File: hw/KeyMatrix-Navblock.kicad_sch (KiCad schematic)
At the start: 52 parts, among them SW4300 SW_Cherry_MX_RGB, SW4301 SW_Cherry_MX_RGB, SW4302 SW_Cherry_MX_RGB, SW4303 SW_Cherry_MX_RGB, SW4304 SW_Cherry_MX_RGB, SW4305 SW_Cherry_MX_RGB, SW4306 SW_Cherry_MX_RGB, SW4307 SW_Cherry_MX_RGB, SW4308 SW_Cherry_MX_RGB, SW4309 SW_Cherry_MX_RGB, SW4310 SW_Cherry_MX_RGB, SW4311 SW_Cherry_MX_RGB, SW4312 SW_Cherry_MX_RGB, SW4313 SW_Cherry_MX_RGB, SW4314 SW_Cherry_MX_RGB, X4300 Keycap-R1-1x1, X4301 Keycap-R1-1x1, X4302 Keycap-R1-1x1, X4303 Keycap-R1-1x1, X4304 Keycap-R1-1x1, X4305 Keycap-R1-1x1, X4306 Keycap-R1-1x1, X4307 Keycap-R1-1x1, X4308 Keycap-R1-1x1, X4309 Keycap-R1-1x1, X4310 Keycap-R1-1x1, X4311 Keycap-R1-1x1, X4312 Keycap-R1-1x1, X4313 Keycap-R1-1x1, X4314 Keycap-R1-1x1

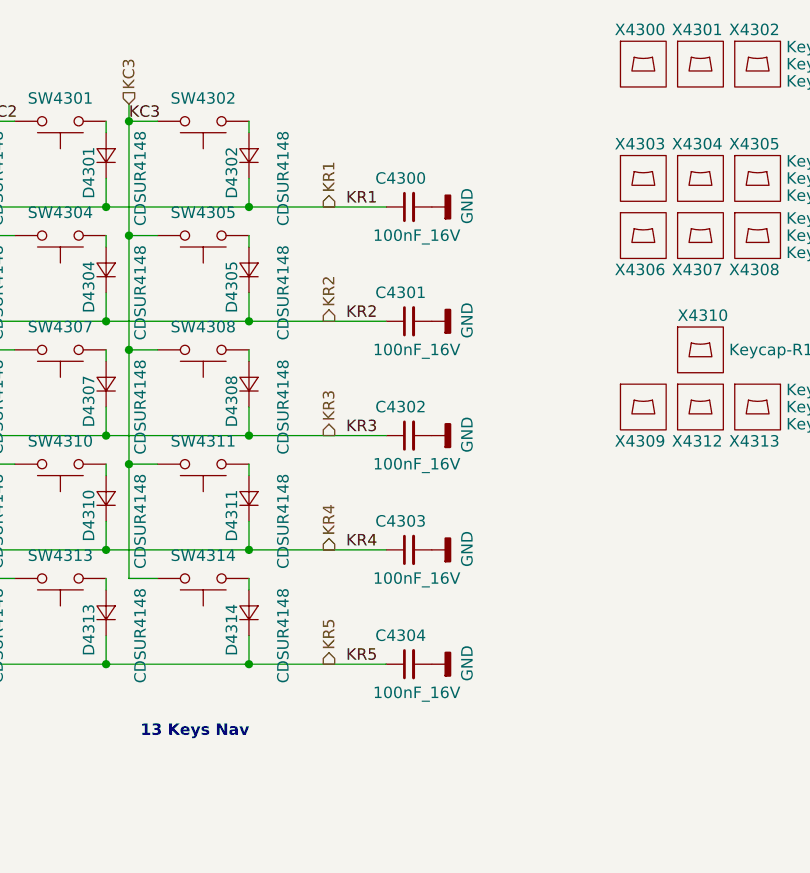
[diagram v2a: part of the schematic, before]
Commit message: Change key matrix capacitors to 220pF.
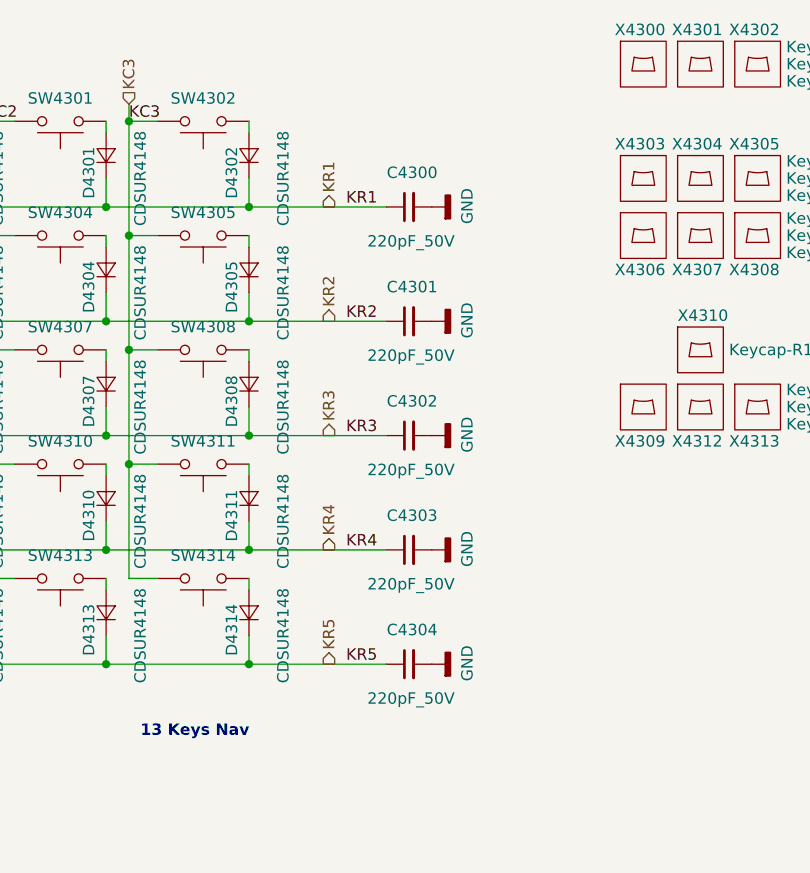
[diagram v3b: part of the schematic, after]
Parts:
- removed C4300, C4301, C4302, C4303, C4304: 100nF_16V, Keyboard:C_0402, symbol Keyboard:100nF_16V
- added C4300, C4301, C4302, C4303, C4304: 220pF_50V, Keyboard:C_0402, symbol Keyboard:220pF_50V
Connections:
- net GND: now also C4300.2, C4301.2, C4302.2, C4303.2, C4304.2
- net KR1: now also C4300.1
- net KR2: now also C4301.1
- net KR3: now also C4302.1
- net KR4: now also C4303.1
- net KR5: now also C4304.1
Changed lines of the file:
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@@
-    (pin "2")
-  )
-  (symbol (lib_id "Keyboard:100nF_16V") (at 88.265 98.425 90) (unit 1)
-    (in_bom yes) (on_board yes)
-    (property "Reference" "C4304" (id 0) (at 90.17 95.25 90)
-      (effects (font (size 1.27 1.27)) (justify left))
-    )
-    (property "Value" "100nF_16V" (id 1) (at 93.98 101.6 90)
-      (effects (font (size 1.27 1.27)) (justify left))
-    )
-    (property "Footprint" "Keyboard:C_0402" (id 2) (at 89.027 100.711 0)
-      (effects (font (size 1.27 1.27)) hide)
-    )
-    (property "Datasheet" "80-C0402C104K4R" (id 3) (at 86.487 98.171 0)
-      (effects (font (size 1.27 1.27)) hide)
-    )
-    (property "mouser#" "80-C0402C104K4R" (id 4) (at 83.947 95.631 0)
-      (effects (font (size 1.524 1.524)) hide)
-    )
-    (pin "1")
     (pin "2")
   )
@@
     (pin "2")
   )
-  (symbol (lib_id "Keyboard:100nF_16V") (at 88.265 60.325 90) (unit 1)
-    (in_bom yes) (on_board yes)
-    (property "Reference" "C4301" (id 0) (at 90.17 57.15 90)
-      (effects (font (size 1.27 1.27)) (justify left))
-    )
-    (property "Value" "100nF_16V" (id 1) (at 93.98 63.5 90)
-      (effects (font (size 1.27 1.27)) (justify left))
-    )
-    (property "Footprint" "Keyboard:C_0402" (id 2) (at 89.027 62.611 0)
-      (effects (font (size 1.27 1.27)) hide)
-    )
-    (property "Datasheet" "80-C0402C104K4R" (id 3) (at 86.487 60.071 0)
-      (effects (font (size 1.27 1.27)) hide)
-    )
-    (property "mouser#" "80-C0402C104K4R" (id 4) (at 83.947 57.531 0)
-      (effects (font (size 1.524 1.524)) hide)
-    )
-    (pin "1")
-    (pin "2")
-  )
   (symbol (lib_id "Keyboard:SW_Cherry_MX_RGB") (at 33.655 38.1 0) (mirror x) (unit 1)
     (in_bom yes) (on_board yes)
@@
     (pin "2")
   )
-  (symbol (lib_id "Keyboard:100nF_16V") (at 88.265 47.625 90) (unit 1)
-    (in_bom yes) (on_board yes)
-    (property "Reference" "C4300" (id 0) (at 90.17 44.45 90)
-      (effects (font (size 1.27 1.27)) (justify left))
-    )
-    (property "Value" "100nF_16V" (id 1) (at 93.98 50.8 90)
-      (effects (font (size 1.27 1.27)) (justify left))
-    )
-    (property "Footprint" "Keyboard:C_0402" (id 2) (at 89.027 49.911 0)
-      (effects (font (size 1.27 1.27)) hide)
-    )
-    (property "Datasheet" "80-C0402C104K4R" (id 3) (at 86.487 47.371 0)
-      (effects (font (size 1.27 1.27)) hide)
-    )
-    (property "mouser#" "80-C0402C104K4R" (id 4) (at 83.947 44.831 0)
-      (effects (font (size 1.524 1.524)) hide)
-    )
-    (pin "1")
-    (pin "2")
-  )
   (symbol (lib_id "Keyboard:GND") (at 90.805 60.325 90) (unit 1)
     (in_bom yes) (on_board yes)
@@
     (pin "2")
   )
-  (symbol (lib_id "Keyboard:100nF_16V") (at 88.265 73.025 90) (unit 1)
-    (in_bom yes) (on_board yes)
-    (property "Reference" "C4302" (id 0) (at 90.17 69.85 90)
-      (effects (font (size 1.27 1.27)) (justify left))
-    )
-    (property "Value" "100nF_16V" (id 1) (at 93.98 76.2 90)
-      (effects (font (size 1.27 1.27)) (justify left))
-    )
-    (property "Footprint" "Keyboard:C_0402" (id 2) (at 89.027 75.311 0)
-      (effects (font (size 1.27 1.27)) hide)
-    )
-    (property "Datasheet" "80-C0402C104K4R" (id 3) (at 86.487 72.771 0)
-      (effects (font (size 1.27 1.27)) hide)
-    )
-    (property "mouser#" "80-C0402C104K4R" (id 4) (at 83.947 70.231 0)
-      (effects (font (size 1.524 1.524)) hide)
-    )
-    (pin "1")
-    (pin "2")
-  )
   (symbol (lib_id "Keyboard:GND") (at 90.805 73.025 90) (unit 1)
     (in_bom yes) (on_board yes)
@@
     (pin "1")
   )
-  (symbol (lib_id "Keyboard:100nF_16V") (at 88.265 85.725 90) (unit 1)
-    (in_bom yes) (on_board yes)
-    (property "Reference" "C4303" (id 0) (at 90.17 82.55 90)
-      (effects (font (size 1.27 1.27)) (justify left))
-    )
-    (property "Value" "100nF_16V" (id 1) (at 93.98 88.9 90)
-      (effects (font (size 1.27 1.27)) (justify left))
-    )
-    (property "Footprint" "Keyboard:C_0402" (id 2) (at 89.027 88.011 0)
-      (effects (font (size 1.27 1.27)) hide)
-    )
-    (property "Datasheet" "80-C0402C104K4R" (id 3) (at 86.487 85.471 0)
-      (effects (font (size 1.27 1.27)) hide)
-    )
-    (property "mouser#" "80-C0402C104K4R" (id 4) (at 83.947 82.931 0)
-      (effects (font (size 1.524 1.524)) hide)
-    )
-    (pin "1")
-    (pin "2")
-  )
   (symbol (lib_id "Keyboard:GND") (at 90.805 85.725 90) (unit 1)
     (in_bom yes) (on_board yes)
@@
     )
     (pin "1")
+  )
+  (symbol (lib_id "Keyboard:220pF_50V") (at 88.265 60.325 90) (unit 1)
+    (in_bom yes) (on_board yes)
+    (property "Reference" "C4301" (id 0) (at 91.44 56.515 90)
+      (effects (font (size 1.27 1.27)) (justify left))
+    )
+    (property "Value" "220pF_50V" (id 1) (at 93.345 64.135 90)
+      (effects (font (size 1.27 1.27)) (justify left))
+    )
+    (property "Footprint" "Keyboard:C_0402" (id 2) (at 89.027 62.611 0)
+      (effects (font (size 1.27 1.27)) hide)
+    )
+    (property "Datasheet" "https://www.mouser.de/datasheet/2/281/1/GRM0335C1H221JA01_01A-1980773.pdf" (id 3) (at 86.487 60.071 0)
+      (effects (font (size 1.27 1.27)) hide)
+    )
+    (property "mouser#" "81-GRM0335C1H221JA1D" (id 4) (at 83.947 57.531 0)
+      (effects (font (size 1.524 1.524)) hide)
+    )
+    (property "manf#" "GRM0335C1H221JA01D" (id 5) (at 88.265 60.325 0)
+      (effects (font (size 1.27 1.27)) hide)
+    )
+    (pin "1")
+    (pin "2")
+  )
+  (symbol (lib_id "Keyboard:220pF_50V") (at 88.265 47.625 90) (unit 1)
+    (in_bom yes) (on_board yes)
+    (property "Reference" "C4300" (id 0) (at 91.44 43.815 90)
+      (effects (font (size 1.27 1.27)) (justify left))
+    )
+    (property "Value" "220pF_50V" (id 1) (at 93.345 51.435 90)
+      (effects (font (size 1.27 1.27)) (justify left))
+    )
+    (property "Footprint" "Keyboard:C_0402" (id 2) (at 89.027 49.911 0)
+      (effects (font (size 1.27 1.27)) hide)
+    )
+    (property "Datasheet" "https://www.mouser.de/datasheet/2/281/1/GRM0335C1H221JA01_01A-1980773.pdf" (id 3) (at 86.487 47.371 0)
+      (effects (font (size 1.27 1.27)) hide)
+    )
+    (property "mouser#" "81-GRM0335C1H221JA1D" (id 4) (at 83.947 44.831 0)
+      (effects (font (size 1.524 1.524)) hide)
+    )
+    (property "manf#" "GRM0335C1H221JA01D" (id 5) (at 88.265 47.625 0)
+      (effects (font (size 1.27 1.27)) hide)
+    )
+    (pin "1")
+    (pin "2")
   )
   (symbol (lib_id "Keyboard:TPD4E02B04") (at 116.84 137.16 0) (unit 1)
@@
     (pin "9")
   )
+  (symbol (lib_id "Keyboard:220pF_50V") (at 88.265 73.025 90) (unit 1)
+    (in_bom yes) (on_board yes)
+    (property "Reference" "C4302" (id 0) (at 91.44 69.215 90)
+      (effects (font (size 1.27 1.27)) (justify left))
+    )
+    (property "Value" "220pF_50V" (id 1) (at 93.345 76.835 90)
+      (effects (font (size 1.27 1.27)) (justify left))
+    )
+    (property "Footprint" "Keyboard:C_0402" (id 2) (at 89.027 75.311 0)
+      (effects (font (size 1.27 1.27)) hide)
+    )
+    (property "Datasheet" "https://www.mouser.de/datasheet/2/281/1/GRM0335C1H221JA01_01A-1980773.pdf" (id 3) (at 86.487 72.771 0)
+      (effects (font (size 1.27 1.27)) hide)
+    )
+    (property "mouser#" "81-GRM0335C1H221JA1D" (id 4) (at 83.947 70.231 0)
+      (effects (font (size 1.524 1.524)) hide)
+    )
+    (property "manf#" "GRM0335C1H221JA01D" (id 5) (at 88.265 73.025 0)
+      (effects (font (size 1.27 1.27)) hide)
+    )
+    (pin "1")
+    (pin "2")
+  )
+  (symbol (lib_id "Keyboard:220pF_50V") (at 88.265 98.425 90) (unit 1)
+    (in_bom yes) (on_board yes)
+    (property "Reference" "C4304" (id 0) (at 91.44 94.615 90)
+      (effects (font (size 1.27 1.27)) (justify left))
+    )
+    (property "Value" "220pF_50V" (id 1) (at 93.345 102.235 90)
+      (effects (font (size 1.27 1.27)) (justify left))
+    )
+    (property "Footprint" "Keyboard:C_0402" (id 2) (at 89.027 100.711 0)
+      (effects (font (size 1.27 1.27)) hide)
+    )
+    (property "Datasheet" "https://www.mouser.de/datasheet/2/281/1/GRM0335C1H221JA01_01A-1980773.pdf" (id 3) (at 86.487 98.171 0)
+      (effects (font (size 1.27 1.27)) hide)
+    )
+    (property "mouser#" "81-GRM0335C1H221JA1D" (id 4) (at 83.947 95.631 0)
+      (effects (font (size 1.524 1.524)) hide)
+    )
+    (property "manf#" "GRM0335C1H221JA01D" (id 5) (at 88.265 98.425 0)
+      (effects (font (size 1.27 1.27)) hide)
+    )
+    (pin "1")
+    (pin "2")
+  )
+  (symbol (lib_id "Keyboard:220pF_50V") (at 88.265 85.725 90) (unit 1)
+    (in_bom yes) (on_board yes)
+    (property "Reference" "C4303" (id 0) (at 91.44 81.915 90)
+      (effects (font (size 1.27 1.27)) (justify left))
+    )
+    (property "Value" "220pF_50V" (id 1) (at 93.345 89.535 90)
+      (effects (font (size 1.27 1.27)) (justify left))
+    )
+    (property "Footprint" "Keyboard:C_0402" (id 2) (at 89.027 88.011 0)
+      (effects (font (size 1.27 1.27)) hide)
+    )
+    (property "Datasheet" "https://www.mouser.de/datasheet/2/281/1/GRM0335C1H221JA01_01A-1980773.pdf" (id 3) (at 86.487 85.471 0)
+      (effects (font (size 1.27 1.27)) hide)
+    )
+    (property "mouser#" "81-GRM0335C1H221JA1D" (id 4) (at 83.947 82.931 0)
+      (effects (font (size 1.524 1.524)) hide)
+    )
+    (property "manf#" "GRM0335C1H221JA01D" (id 5) (at 88.265 85.725 0)
+      (effects (font (size 1.27 1.27)) hide)
+    )
+    (pin "1")
+    (pin "2")
+  )
   (symbol (lib_id "Keyboard:TPD4E02B04") (at 72.39 137.16 0) (unit 1)
